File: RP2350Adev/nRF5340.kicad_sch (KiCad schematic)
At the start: 29 parts, among them J1 J-Link, J2 SPI Pins, J3 QSPI Pins, J4 UART Pins, U1 nRF5340-QKxx, X1 32.768kHz, X2 32MHz

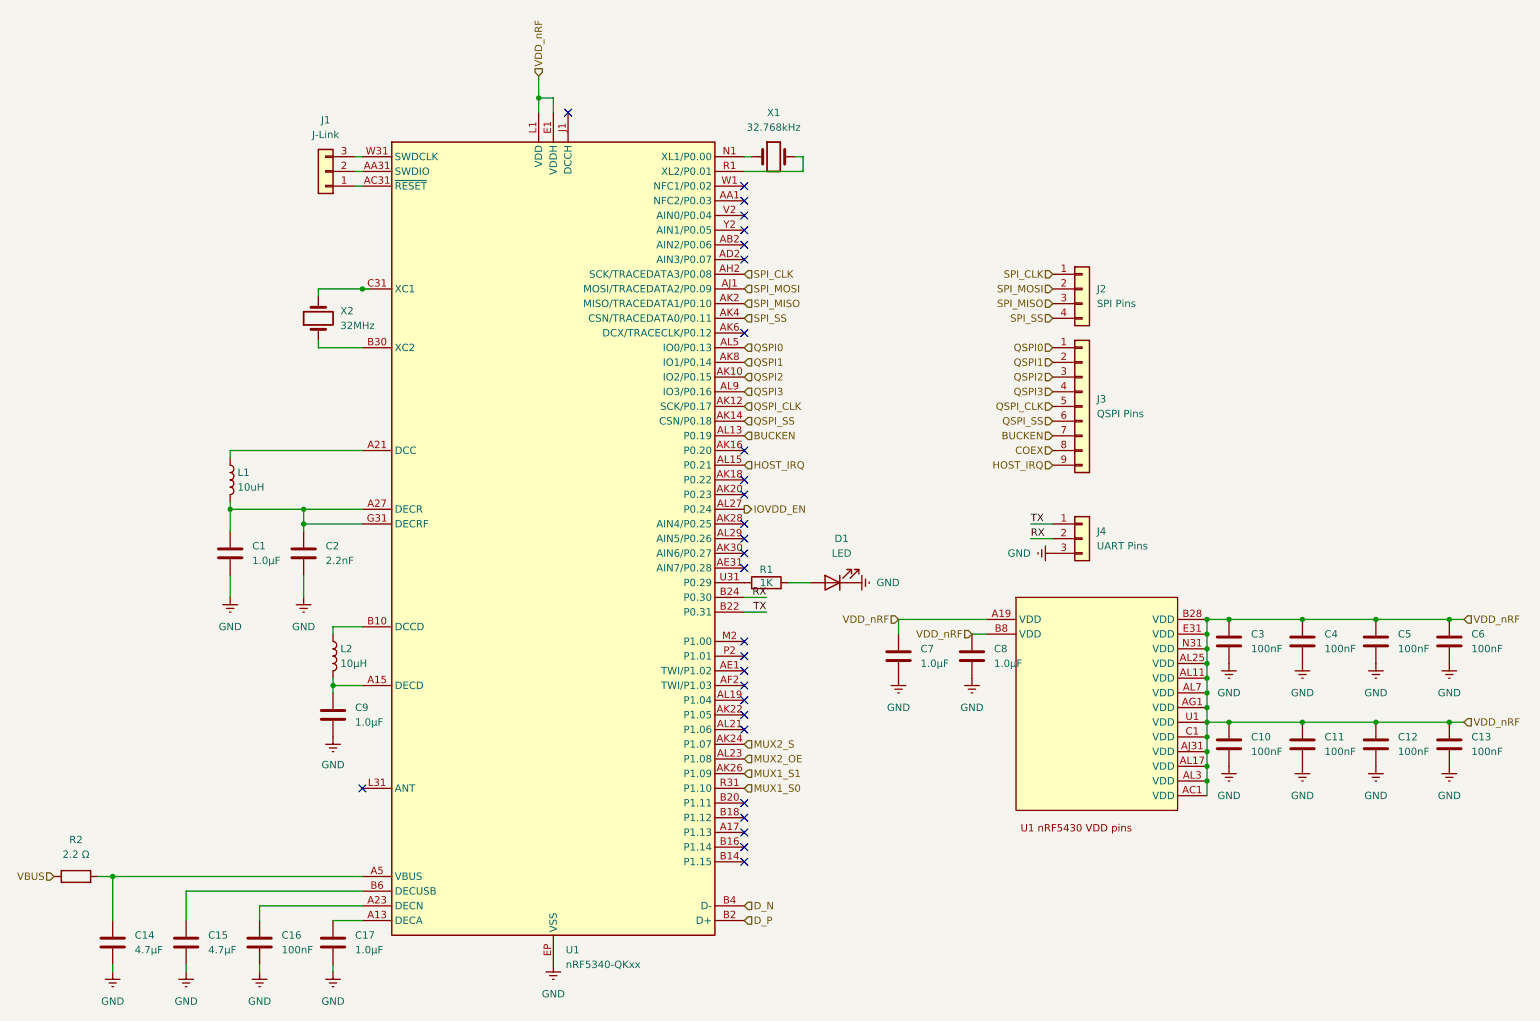
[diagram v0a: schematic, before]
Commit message: Layout Assembly Attempt (Components not being transferred as expected, major issues)
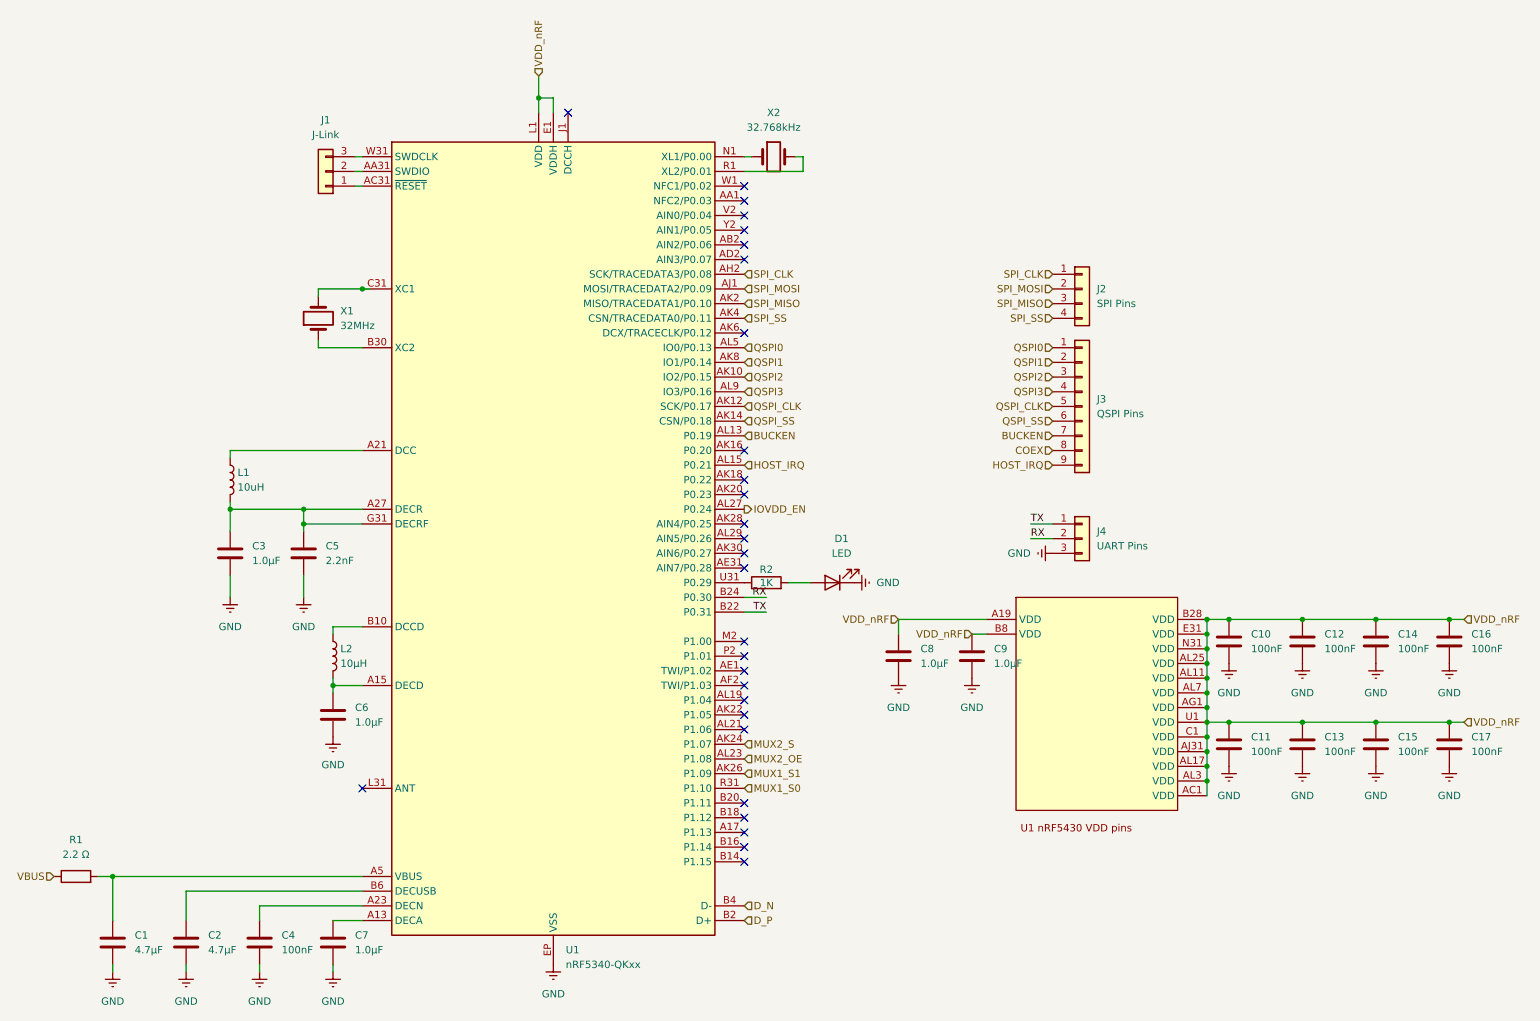
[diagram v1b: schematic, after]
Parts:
- renumbered C14 to C1, C3 to C10, C10 to C11, C4 to C12, C11 to C13, C5 to C14, C12 to C15, C6 to C16, C13 to C17, C15 to C2, C1 to C3, C16 to C4, C2 to C5, C9 to C6, C17 to C7, C7 to C8, C8 to C9, R2 to R1, R1 to R2, X2 to X1, X1 to X2

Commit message: Combine subcircuits
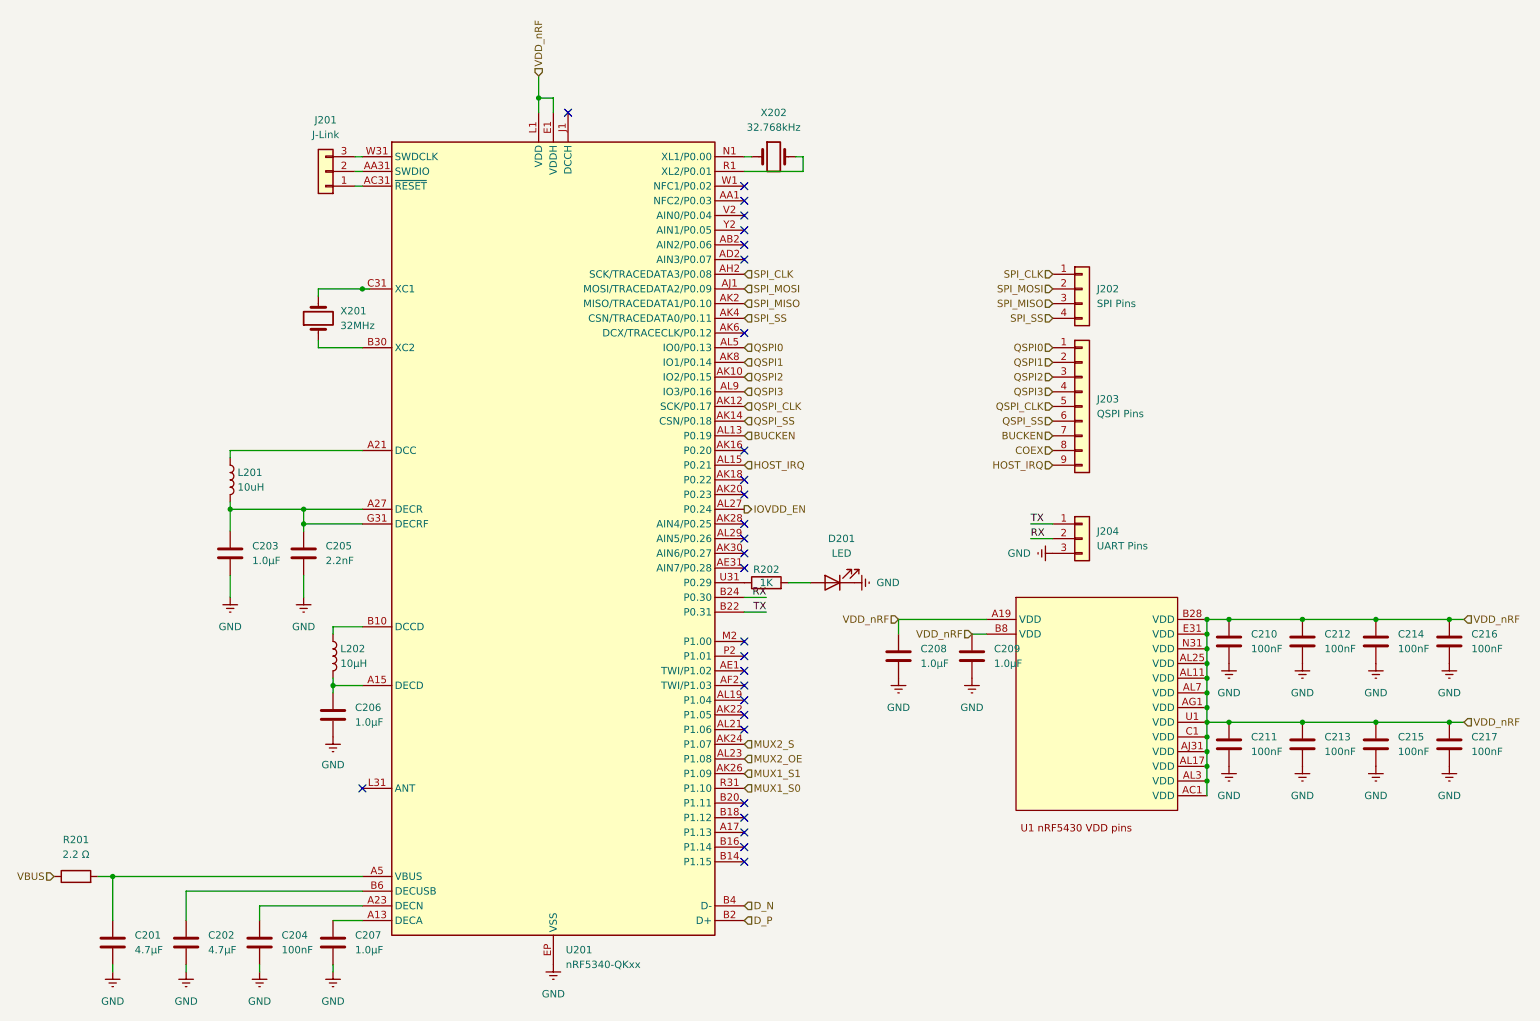
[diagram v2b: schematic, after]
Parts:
- renumbered C1 to C201, C2 to C202, C3 to C203, C4 to C204, C5 to C205, C6 to C206, C7 to C207, C8 to C208, C9 to C209, C10 to C210, C11 to C211, C12 to C212, C13 to C213, C14 to C214, C15 to C215, C16 to C216, C17 to C217, D1 to D201, J1 to J201, J2 to J202, J3 to J203, J4 to J204, L1 to L201, L2 to L202, R1 to R201, R2 to R202, U1 to U201, X1 to X201, X2 to X202

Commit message: RF layout
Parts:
- U201: footprint Package_DFN_QFN:Nordic_AQFN-94-1EP_7x7mm_P0.4mm -> Eclectronics:Nordic_AQFN-94-1EP_7x7mm_P0.4mm
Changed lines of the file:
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@@
 			)
 		)
-		(property "Footprint" "Package_DFN_QFN:Nordic_AQFN-94-1EP_7x7mm_P0.4mm"
+		(property "Footprint" "Eclectronics:Nordic_AQFN-94-1EP_7x7mm_P0.4mm"
 			(at 142.24 35.56 0)
 			(effects

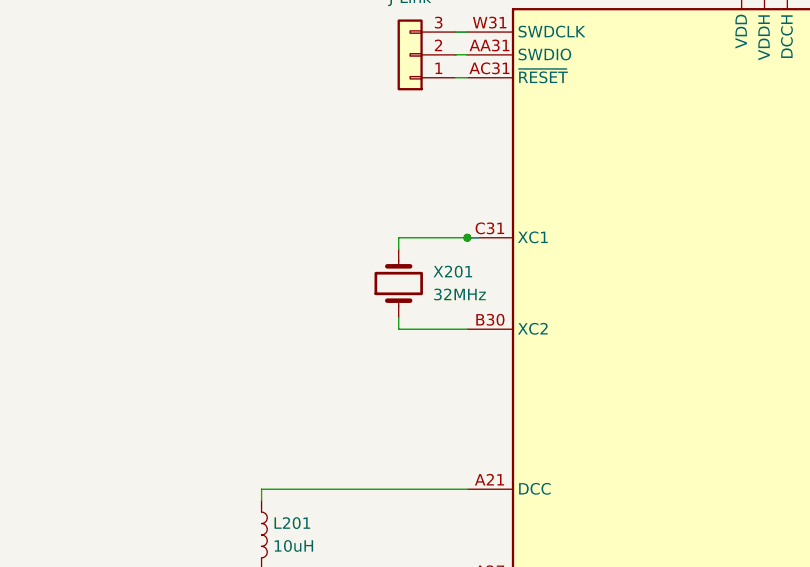
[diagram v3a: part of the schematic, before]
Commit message: fix footprint errors
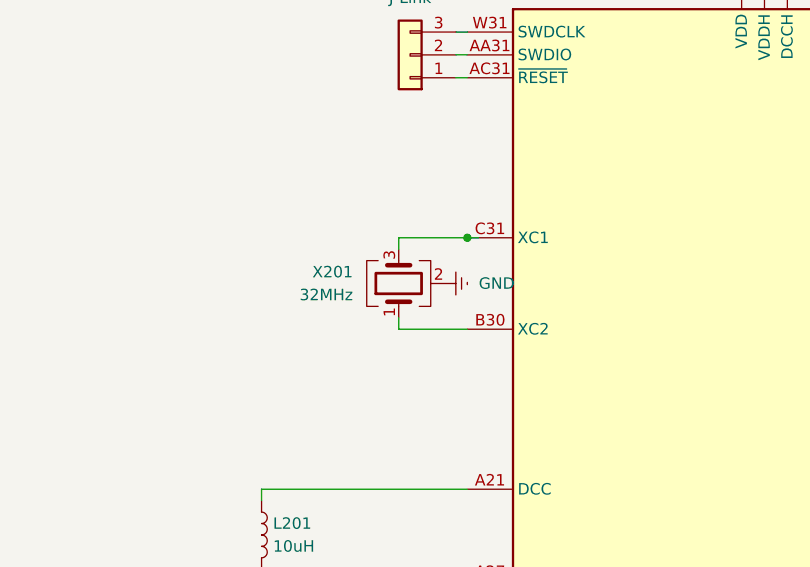
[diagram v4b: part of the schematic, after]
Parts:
- X201: symbol Device:Crystal -> Device:Crystal_GND24
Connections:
- net GND: now also X201.2 (G), X201.4 (G)
- net at U201.C31 (XC1): now also X201.3; no longer X201.2
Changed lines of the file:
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@@
 	)
 	(symbol
-		(lib_id "Device:Crystal")
+		(lib_id "Device:Crystal_GND24")
 		(at 66.04 71.12 90)
 		(unit 1)
@@
 		(fields_autoplaced yes)
 		(property "Reference" "X201"
-			(at 69.85 69.8499 90)
-			(effects
-				(font
-					(size 1.27 1.27)
-				)
-				(justify right)
+			(at 60.96 69.8499 90)
+			(effects
+				(font
+					(size 1.27 1.27)
+				)
+				(justify left)
 			)
 		)
 		(property "Value" "32MHz"
-			(at 69.85 72.3899 90)
-			(effects
-				(font
-					(size 1.27 1.27)
-				)
-				(justify right)
+			(at 60.96 72.3899 90)
+			(effects
+				(font
+					(size 1.27 1.27)
+				)
+				(justify left)
 			)
 		)
@@
 			)
 		)
-		(property "Description" "Two pin crystal"
+		(property "Description" "Four pin crystal, GND on pins 2 and 4"
 			(at 66.04 71.12 0)
 			(effects
@@
 		)
 		(pin "2"
+		)
+		(pin "3"
+		)
+		(pin "4"
 		)
 		(instances
@@
 					(unit 1)
 				)
+			)
+		)
+	)
+	(symbol
+		(lib_id "power:GNDREF")
+		(at 71.12 71.12 90)
+		(unit 1)
+		(exclude_from_sim no)
+		(in_bom yes)
+		(on_board yes)
+		(dnp no)
+		(fields_autoplaced yes)
+		(property "Reference" "#PWR01"
+			(at 77.47 71.12 0)
+			(effects
+				(font
+					(size 1.27 1.27)
+				)
+				(hide yes)
+			)
+		)
+		(property "Value" "GND"
+			(at 74.93 71.1199 90)
+			(effects
+				(font
+					(size 1.27 1.27)
+				)
+				(justify right)
+			)
+		)
+		(property "Footprint" ""
+			(at 71.12 71.12 0)
+			(effects
+				(font
+					(size 1.27 1.27)
+				)
+				(hide yes)
+			)
+		)
+		(property "Datasheet" ""
+			(at 71.12 71.12 0)
+			(effects
+				(font
+					(size 1.27 1.27)
+				)
+				(hide yes)
+			)
+		)
+		(property "Description" "Power symbol creates a global label with name \"GNDREF\" , reference supply ground"
+			(at 71.12 71.12 0)
+			(effects
+				(font
+					(size 1.27 1.27)
+				)
+				(hide yes)
+			)
+		)
+		(pin "1"
+		)
+		(instances
+			(project "main"
+				(path "/1f57b86c-11e7-4ea8-8f36-592c0861a25b/52f2bb31-32ae-4b06-aca7-93e1eef009d8"
+					(reference "#PWR01")
+					(unit 1)
+				)
